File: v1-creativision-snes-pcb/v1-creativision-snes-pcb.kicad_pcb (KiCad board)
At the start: 2 copper layers, 66 x 64 mm, 6 parts, among them J1 Conn_01x10_Pin, J2 Conn_01x10_Pin, J3 Power Entry, J4 PS/2 Keyboard, J5 SNES, U1 Pico

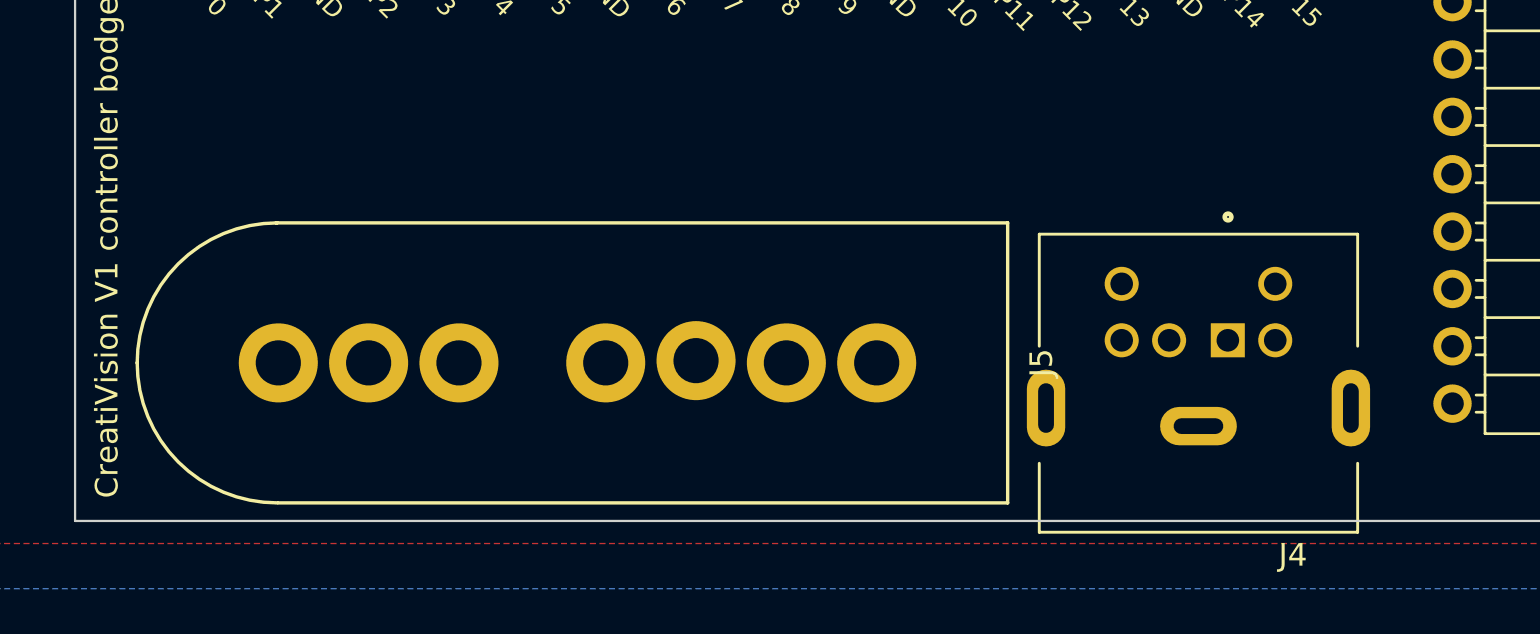
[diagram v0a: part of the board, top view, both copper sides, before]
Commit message: Swap keyboard and SFC for strain relief
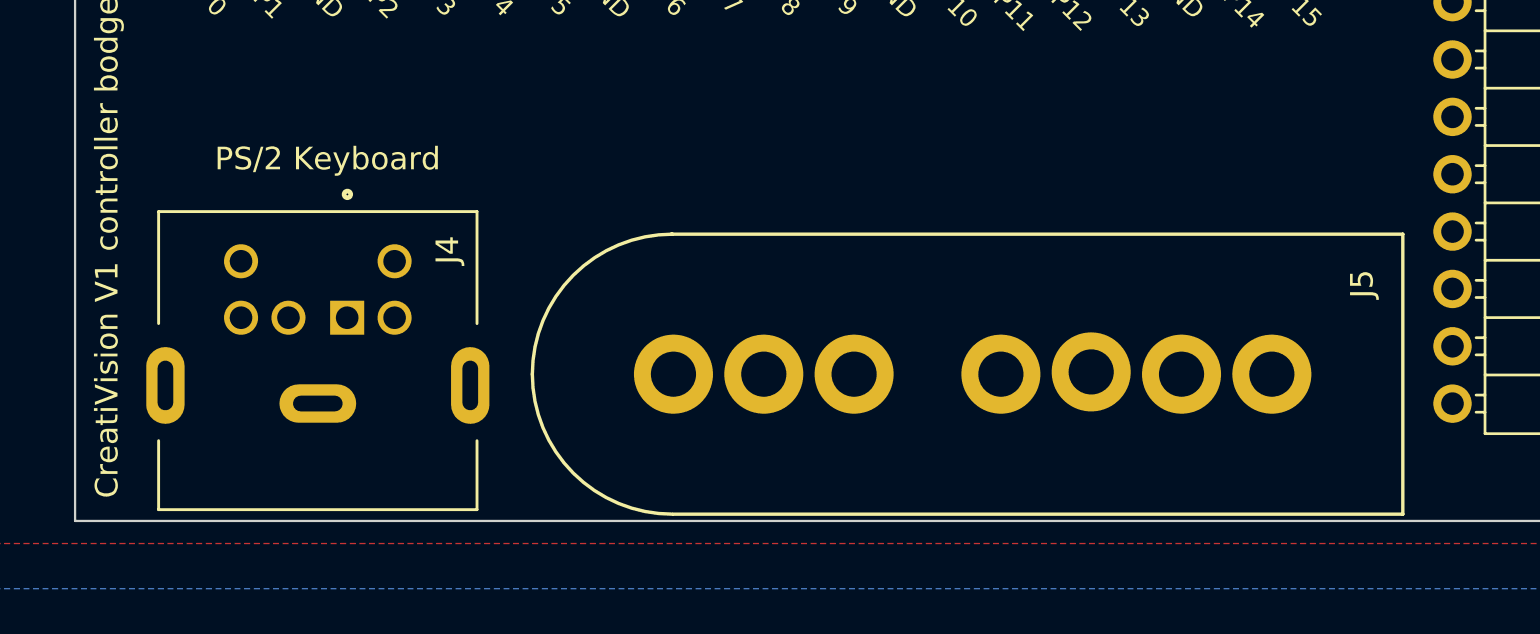
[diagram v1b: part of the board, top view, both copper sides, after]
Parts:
- moved J4 39.0 mm to (103.8, 88.6)
- moved J5 17.5 mm to (134.0, 89.5)
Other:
- board text added: "Clk"
- board text added: "Clock"
- board text added: "Data"
- board text added: "Latch"
- board text added: "Serial"
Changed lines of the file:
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@@
   (net 66 "unconnected-(U1-SWDIO-Pad43)")
   (footprint "imciner2-connectors:GAMING_SNES" (layer "F.Cu")
-    (at 116.5 89 180)
+    (at 134 89.5 180)
     (property "Sheetfile" "v1-creativision-snes-pcb.kicad_sch")
     (property "Sheetname" "")
@@
     (property "ki_keywords" "connector")
     (attr through_hole)
-    (fp_text reference "J5" (at -19.3 0 90) (layer "F.SilkS")
+    (fp_text reference "J5" (at -16 4 90) (layer "F.SilkS")
         (effects (font (size 1 1) (thickness 0.15)))
     )
@@
   )
   (footprint "MD-60FC:CUI_MD-60FC" (layer "F.Cu")
-    (at 142.75 89.57 180)
+    (at 103.75 88.57 180)
     (property "Sheetfile" "v1-creativision-snes-pcb.kicad_sch")
     (property "Sheetname" "")
@@
     (property "ki_keywords" "Mini-DIN")
     (attr through_hole)
-    (fp_text reference "J4" (at -4.18605 -7.947) (layer "F.SilkS")
+    (fp_text reference "J4" (at -5.75 4.57 90) (layer "F.SilkS")
         (effects (font (size 1.000252 1.000252) (thickness 0.15)))
     )
-    (fp_text value "PS/2 Keyboard" (at -0.43503 8.60555) (layer "F.Fab")
+    (fp_text value "PS/2 Keyboard" (at -0.43503 8.60555) (layer "F.SilkS")
         (effects (font (size 1.000063 1.000063) (thickness 0.15)))
     )
@@
   (gr_line (start 100 32) (end 93 39)
     (stroke (width 0.1) (type default)) (layer "Edge.Cuts"))
+  (gr_text "Data" (at 105.5 82 90) (layer "B.SilkS")
+    (effects (font (size 1 1) (thickness 0.15)) (justify left bottom mirror))
+  )
+  (gr_text "Clk" (at 103 83 90) (layer "B.SilkS")
+    (effects (font (size 1 1) (thickness 0.15)) (justify left bottom mirror))
+  )
+  (gr_text "Clock" (at 142.5 82.5 90) (layer "B.SilkS")
+    (effects (font (size 1 1) (thickness 0.15)) (justify left bottom mirror))
+  )
+  (gr_text "Serial" (at 134.5 82.5 90) (layer "B.SilkS")
+    (effects (font (size 1 1) (thickness 0.15)) (justify left bottom mirror))
+  )
+  (gr_text "Latch" (at 138.5 82.5 90) (layer "B.SilkS")
+    (effects (font (size 1 1) (thickness 0.15)) (justify left bottom mirror))
+  )
   (gr_text "GND" (at 146 40 90) (layer "F.SilkS")
     (effects (font (size 1 1) (thickness 0.15)) (justify left bottom))

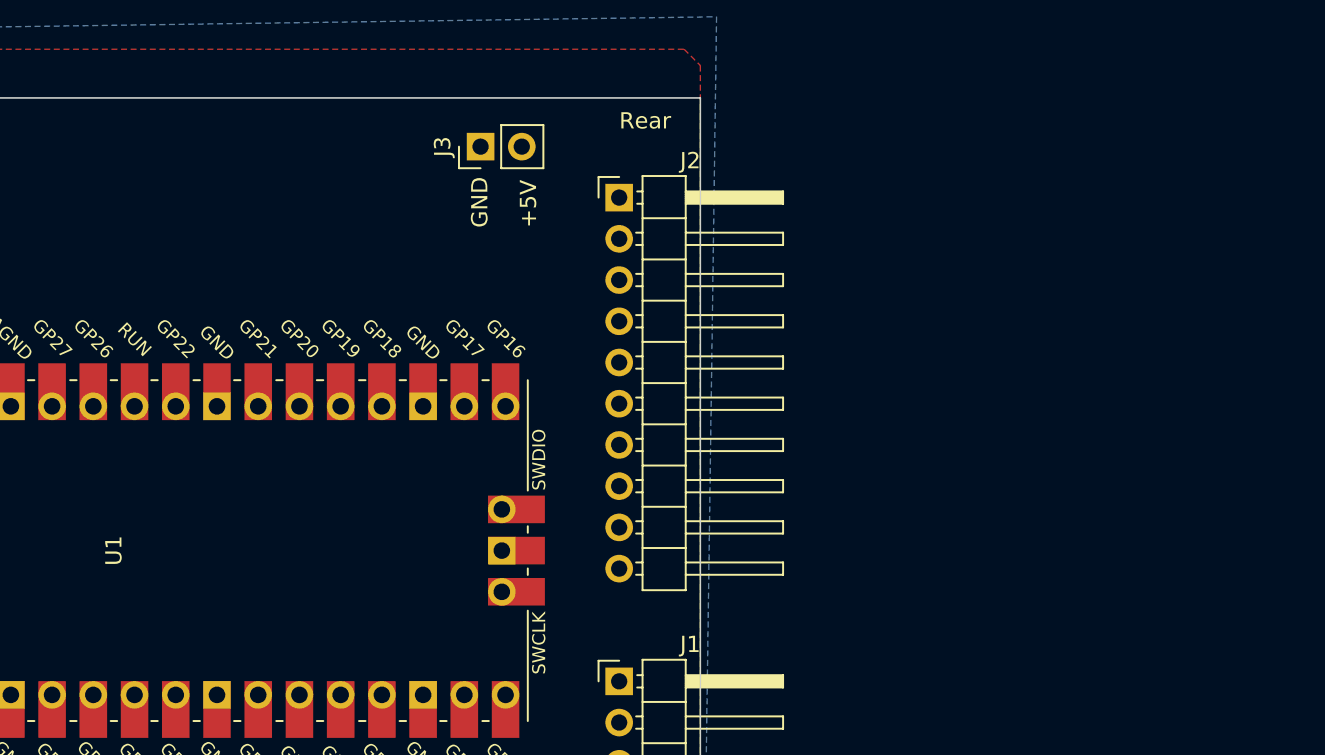
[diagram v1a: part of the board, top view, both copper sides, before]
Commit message: Use 74lvc245 instead of voltage divider
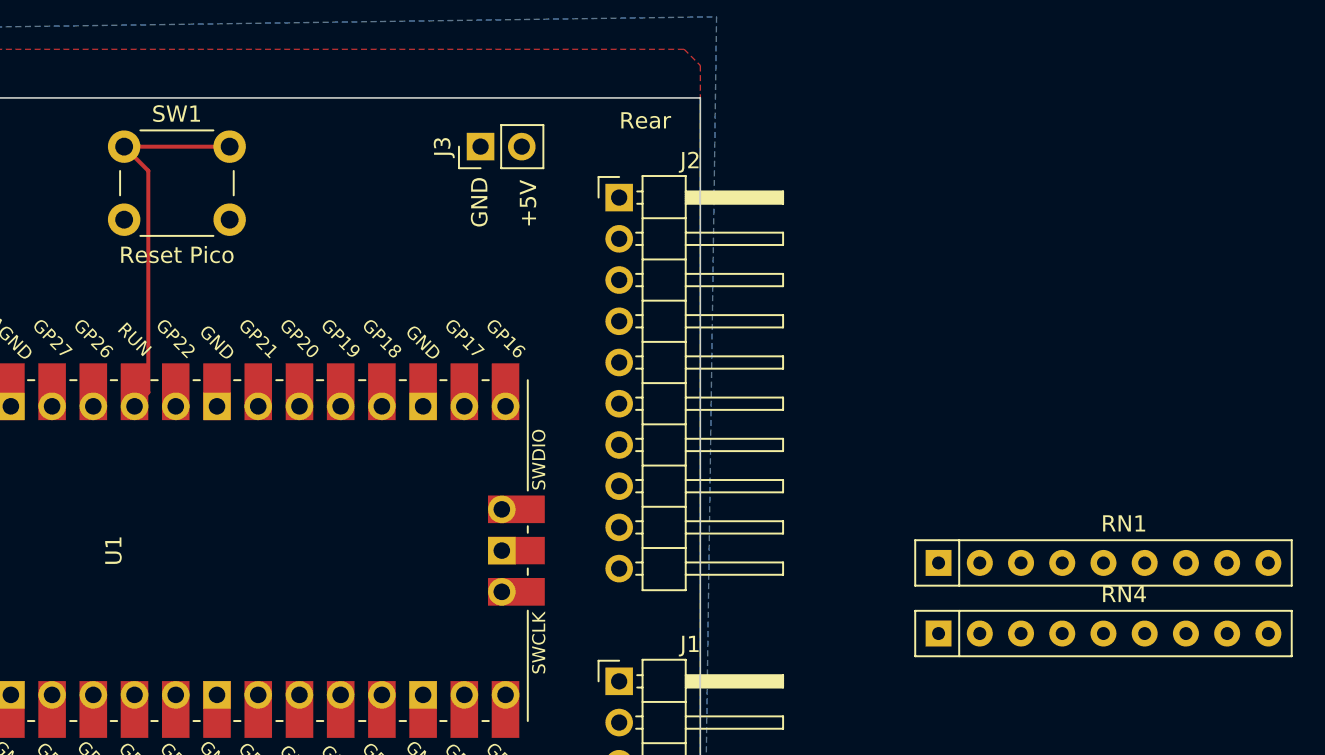
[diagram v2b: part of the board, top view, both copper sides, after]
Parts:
- added RN1: 20kΩ, Resistor_THT:R_Array_SIP9, F.Cu at (173.7, 60.6)
- added RN4: 20kΩ, Resistor_THT:R_Array_SIP9, F.Cu at (173.7, 65.0)
- added SW1: Reset Pico, Button_Switch_THT:SW_PUSH_6mm, F.Cu at (123.5, 35.0)
- J1: value Conn_01x10_Pin -> Left Joystick
- J2: value Conn_01x10_Pin -> Right Joystick
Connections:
- J1 pad 1: unconnected-(J1-Pin_1-Pad1) -> /LeftA
- J1 pad 10: unconnected-(J1-Pin_10-Pad10) -> /PA2
- J1 pad 2: unconnected-(J1-Pin_2-Pad2) -> /LeftB
- J1 pad 3: unconnected-(J1-Pin_3-Pad3) -> /LeftC
- J1 pad 4: unconnected-(J1-Pin_4-Pad4) -> /LeftD
- J1 pad 5: unconnected-(J1-Pin_5-Pad5) -> /LeftE
- J1 pad 6: unconnected-(J1-Pin_6-Pad6) -> /LeftF
- J1 pad 7: unconnected-(J1-Pin_7-Pad7) -> /LeftG
- J1 pad 8: unconnected-(J1-Pin_8-Pad8) -> /LeftH
- J1 pad 9: unconnected-(J1-Pin_9-Pad9) -> /PA3
- J2 pad 1: unconnected-(J2-Pin_1-Pad1) -> /PA1
- J2 pad 10: unconnected-(J2-Pin_10-Pad10) -> /RightH
- J2 pad 2: unconnected-(J2-Pin_2-Pad2) -> /PA0
- J2 pad 3: unconnected-(J2-Pin_3-Pad3) -> /RightA
- J2 pad 4: unconnected-(J2-Pin_4-Pad4) -> /RightB
- J2 pad 5: unconnected-(J2-Pin_5-Pad5) -> /RightC
- J2 pad 6: unconnected-(J2-Pin_6-Pad6) -> /RightD
- J2 pad 7: unconnected-(J2-Pin_7-Pad7) -> /RightE
- J2 pad 8: unconnected-(J2-Pin_8-Pad8) -> /RightF
- J2 pad 9: unconnected-(J2-Pin_9-Pad9) -> /RightG
- U1 pad 1: unconnected-(U1-GPIO0-Pad1) -> /PA0
- U1 pad 10: unconnected-(U1-GPIO7-Pad10) -> Net-(RN1-R4)
- U1 pad 11: unconnected-(U1-GPIO8-Pad11) -> Net-(RN1-R5)
- U1 pad 12: unconnected-(U1-GPIO9-Pad12) -> Net-(RN1-R6)
- U1 pad 14: unconnected-(U1-GPIO10-Pad14) -> Net-(RN1-R7)
- U1 pad 15: unconnected-(U1-GPIO11-Pad15) -> Net-(RN1-R8)
- U1 pad 16: unconnected-(U1-GPIO12-Pad16) -> Net-(RN3-R1.2)
- U1 pad 17: unconnected-(U1-GPIO13-Pad17) -> Net-(RN3-R2.2)
- U1 pad 19: unconnected-(U1-GPIO14-Pad19) -> Net-(RN3-R3.2)
- U1 pad 2: unconnected-(U1-GPIO1-Pad2) -> /PA1
- U1 pad 20: unconnected-(U1-GPIO15-Pad20) -> Net-(RN3-R4.2)
- U1 pad 21: unconnected-(U1-GPIO16-Pad21) -> Net-(RN3-R5.2)
- U1 pad 22: unconnected-(U1-GPIO17-Pad22) -> Net-(RN3-R6.2)
- U1 pad 24: unconnected-(U1-GPIO18-Pad24) -> Net-(RN3-R7.2)
- U1 pad 25: unconnected-(U1-GPIO19-Pad25) -> Net-(RN3-R8.2)
- U1 pad 26: unconnected-(U1-GPIO20-Pad26) -> /SNES_Clock
- U1 pad 27: unconnected-(U1-GPIO21-Pad27) -> /SNES_Latch
- U1 pad 29: unconnected-(U1-GPIO22-Pad29) -> /SNES_Serial
- U1 pad 30: unconnected-(U1-RUN-Pad30) -> Net-(U1-RUN)
- U1 pad 32: unconnected-(U1-GPIO27_ADC1-Pad32) -> /PS2_CLK
- U1 pad 34: unconnected-(U1-GPIO28_ADC2-Pad34) -> /PS2_DATA
- U1 pad 39: unconnected-(U1-VSYS-Pad39) -> +5V
- U1 pad 4: unconnected-(U1-GPIO2-Pad4) -> /PA2
- U1 pad 5: unconnected-(U1-GPIO3-Pad5) -> /PA3
- U1 pad 6: unconnected-(U1-GPIO4-Pad6) -> Net-(RN1-R1)
- U1 pad 7: unconnected-(U1-GPIO5-Pad7) -> Net-(RN1-R2)
- U1 pad 9: unconnected-(U1-GPIO6-Pad9) -> Net-(RN1-R3)
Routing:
- net Net-(U1-RUN): track 0.00 -> 23.5 mm
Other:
- board text added: "Left"
- board text added: "PA0"
- board text added: "PA1"
- board text added: "PA2"
- board text added: "PA3"
- board text added: "Right"

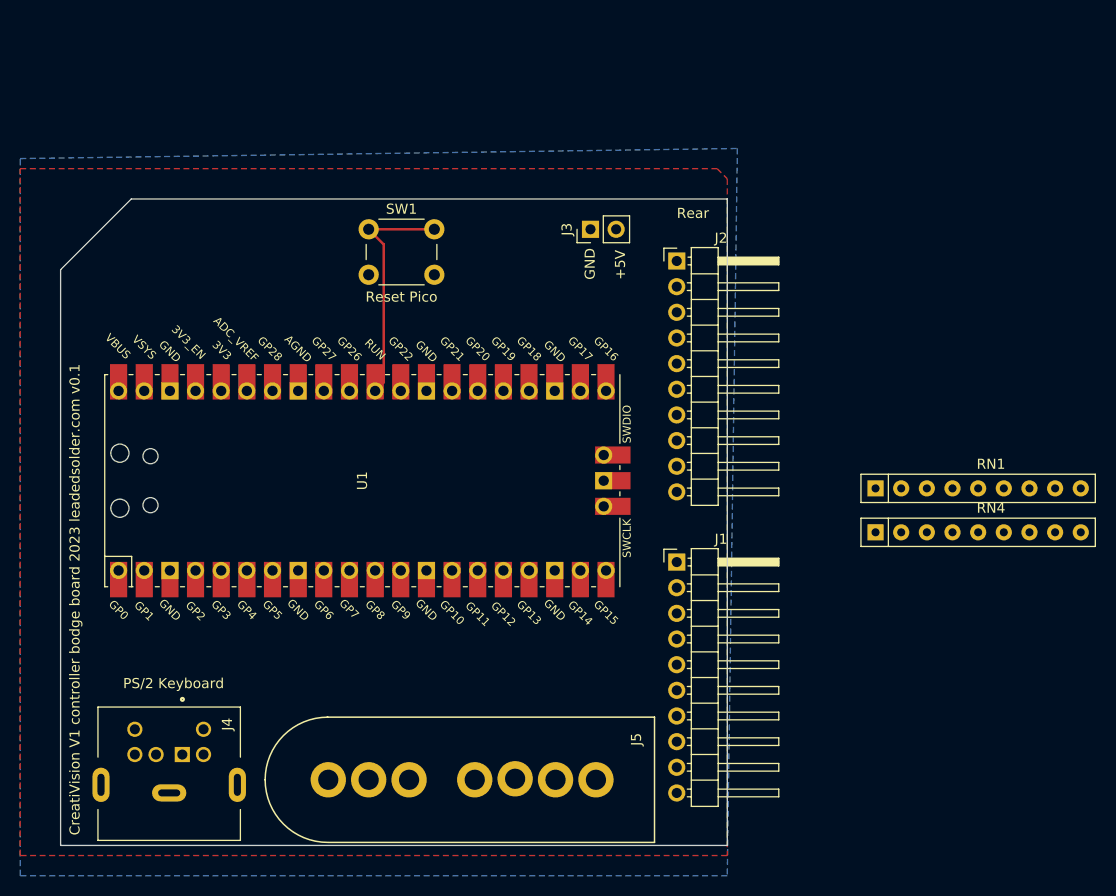
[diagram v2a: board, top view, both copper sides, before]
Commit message: PCB all joined up with the lvc strategy
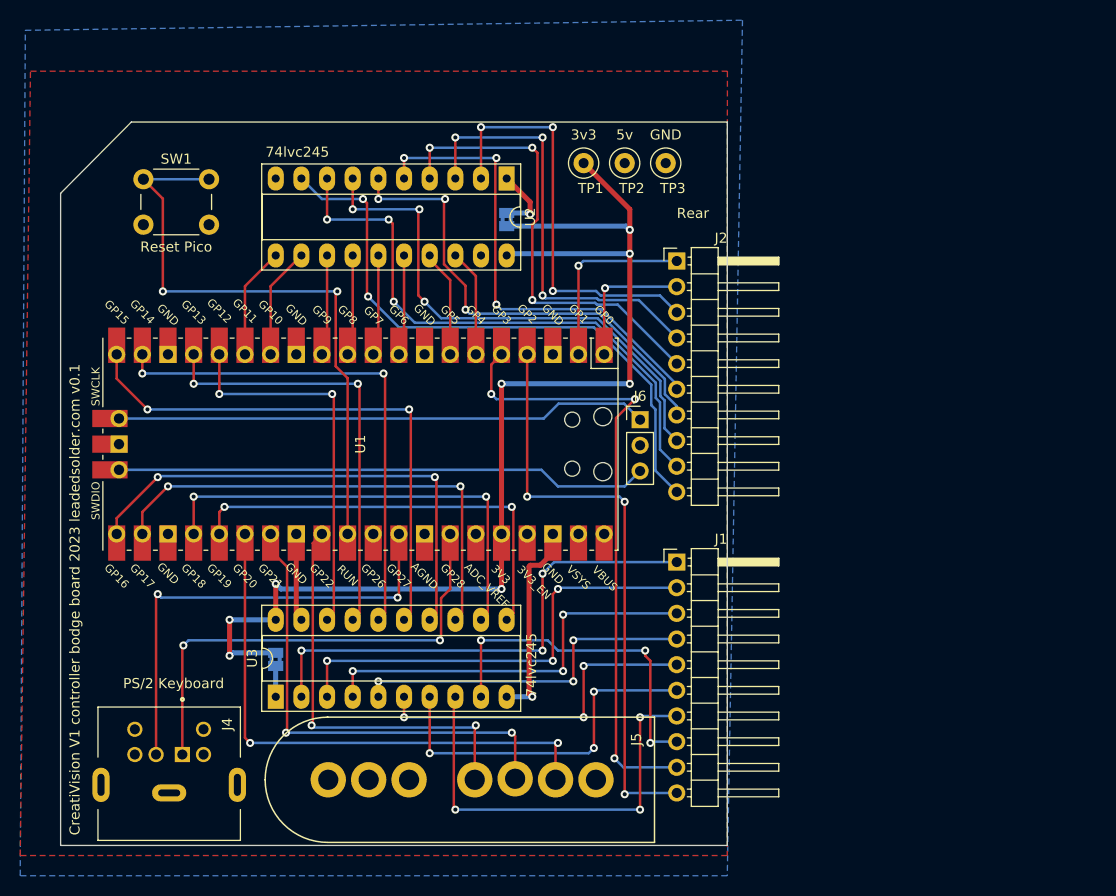
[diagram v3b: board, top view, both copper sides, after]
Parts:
- removed J3: Power Entry, Connector_PinHeader_2.54mm:PinHeader_1x02_P2.54mm_Vertical
- removed RN1, RN4: 20kΩ, Resistor_THT:R_Array_SIP9
- added J6: Debug, Connector_PinHeader_2.54mm:PinHeader_1x03_P2.54mm_Vertical, F.Cu at (150.4, 53.8)
- added JP1: Jumper_2_Bridged, Jumper:SolderJumper-2_P1.3mm_Bridged2Bar_Pad1.0x1.5mm, B.Cu at (114.3, 77.6)
- added JP2: Jumper_2_Bridged, Jumper:SolderJumper-2_P1.3mm_Bridged2Bar_Pad1.0x1.5mm, B.Cu at (137.2, 34.0)
- added TP1: 3v3, TestPoint:TestPoint_Loop_D1.80mm_Drill1.0mm_Beaded, F.Cu at (144.8, 28.4)
- added TP2: 5v, TestPoint:TestPoint_Loop_D1.80mm_Drill1.0mm_Beaded, F.Cu at (148.8, 28.4)
- added TP3: GND, TestPoint:TestPoint_Loop_D1.80mm_Drill1.0mm_Beaded, F.Cu at (152.9, 28.4)
- added U2: TRANSCEIVER-8BIT, Package_DIP:DIP-20_W7.62mm_Socket_LongPads, F.Cu at (137.2, 30.0)
- added U3: TRANSCEIVER-8BIT, Package_DIP:DIP-20_W7.62mm_Socket_LongPads, F.Cu at (114.3, 81.3)
- moved SW1 22.8 mm to (101.2, 30.0)
- moved U1 3.62 mm to (122.7, 56.3), turned to -90 degrees
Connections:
- U1 pad 36: unconnected-(U1-3V3-Pad36) -> +3.3V
- U1 pad 41: unconnected-(U1-SWCLK-Pad41) -> /SWCLK
- U1 pad 43: unconnected-(U1-SWDIO-Pad43) -> /SWDIO
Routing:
- net +3.3V: track 0.00 -> 120.3 mm, vias 0 -> 8
- net /PA3: track 0.00 -> 61.7 mm, vias 0 -> 3
- net /RightH: track 0.00 -> 60.1 mm, vias 0 -> 2
- net /PA2: track 0.00 -> 58.1 mm, vias 0 -> 3
- net /RightG: track 0.00 -> 56.9 mm, vias 0 -> 3
- net /SNES_Clock: track 0.00 -> 55.1 mm, vias 0 -> 2
- net Net-(U1-GPIO15): track 0.00 -> 53.8 mm, vias 0 -> 2
- net /SWDIO: track 0.00 -> 52.9 mm
- net /SWCLK: track 0.00 -> 52.8 mm
- net /RightF: track 0.00 -> 52.3 mm, vias 0 -> 3
- net Net-(U1-GPIO14): track 0.00 -> 50.5 mm, vias 0 -> 2
- net /LeftA: track 0.00 -> 49.8 mm, vias 0 -> 3
- net Net-(U1-GPIO16): track 0.00 -> 49.3 mm, vias 0 -> 2
- net Net-(U1-GPIO17): track 0.00 -> 48.3 mm, vias 0 -> 2
- net /SNES_Latch: track 0.00 -> 47.4 mm, vias 0 -> 2
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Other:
- board size 66 x 64 mm -> 66 x 71.6 mm
- board text added: "74lvc245"
- board text removed: "+5V"
- board text removed: "GND"
